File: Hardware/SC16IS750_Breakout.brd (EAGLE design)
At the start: 27.9 x 22.9 mm, 17 parts, among them IC1 SC16IS750, Q1 14.7456MHz, U1 3.3V

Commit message: Fixed board files
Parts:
- added U$2: (no value), SparkFun-Aesthetics:CREATIVE_COMMONS
- C1, C2, C4: device SparkFun:0402-CAP -> SparkFun-Passives:0603-CAP
- IC1: device SparkFun:QFN-24 -> SparkFun-DigitalIC:QFN-24
- R1, R2, R3: device SparkFun:0402-RES -> SparkFun-Passives:0603-RES
- moved C2 1.27 mm to (5.08, 14.0)
- moved R1 1.00 mm to (10.2, 12.4)
- turned C1 to 90 degrees
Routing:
- net N$24: track 9.98 -> 12.3 mm
- net N$23: track 11.0 -> 12.4 mm
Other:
- board text added: "C. Taylor, Updated by: T. Klopfenstein"

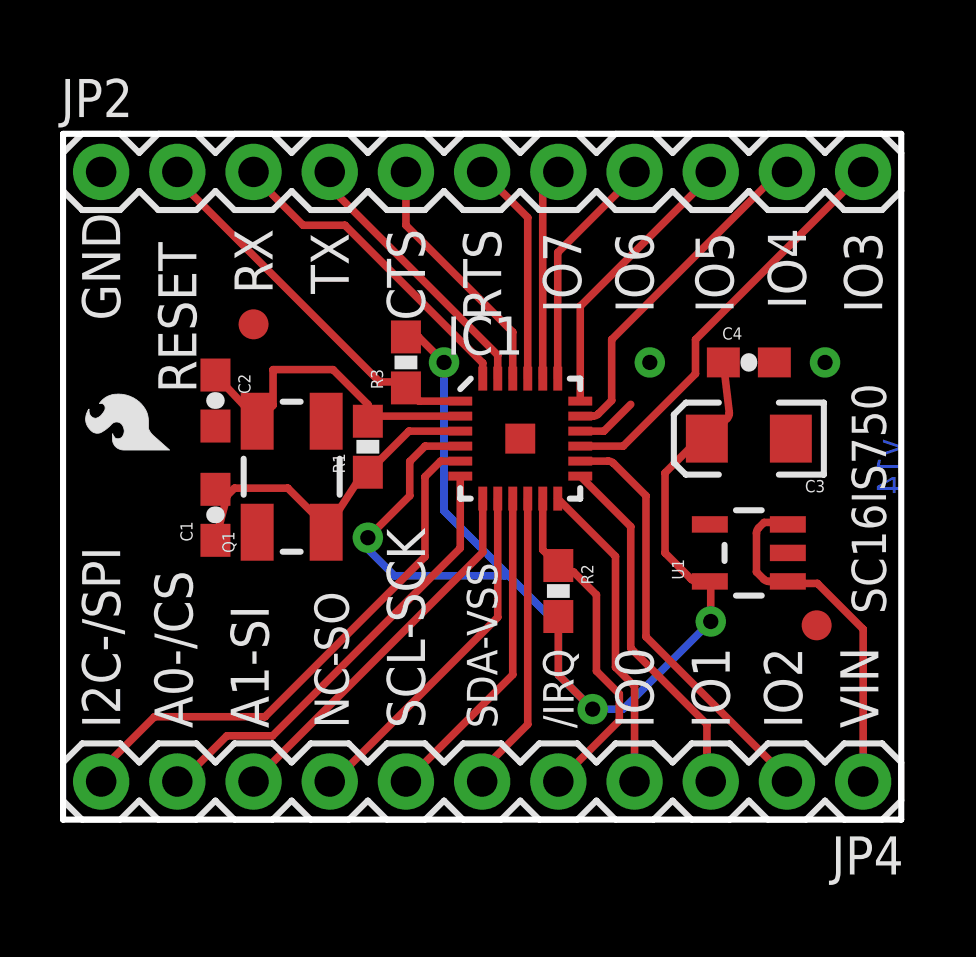
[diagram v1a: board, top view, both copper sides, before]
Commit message: Fixed traces that were crooked
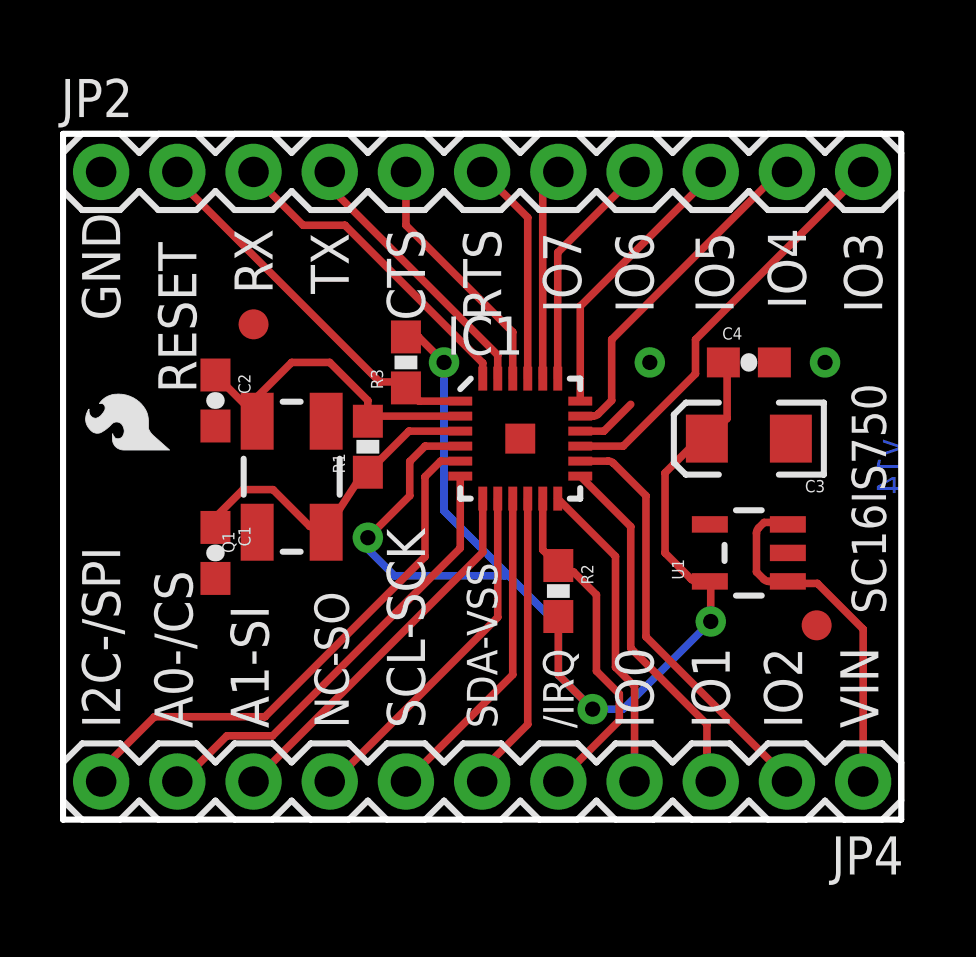
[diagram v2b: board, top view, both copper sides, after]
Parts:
- moved C1 1.27 mm to (5.08, 8.89), turned to 270 degrees

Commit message: Updated Package to "1:1" and rerouted traces directly away from IC
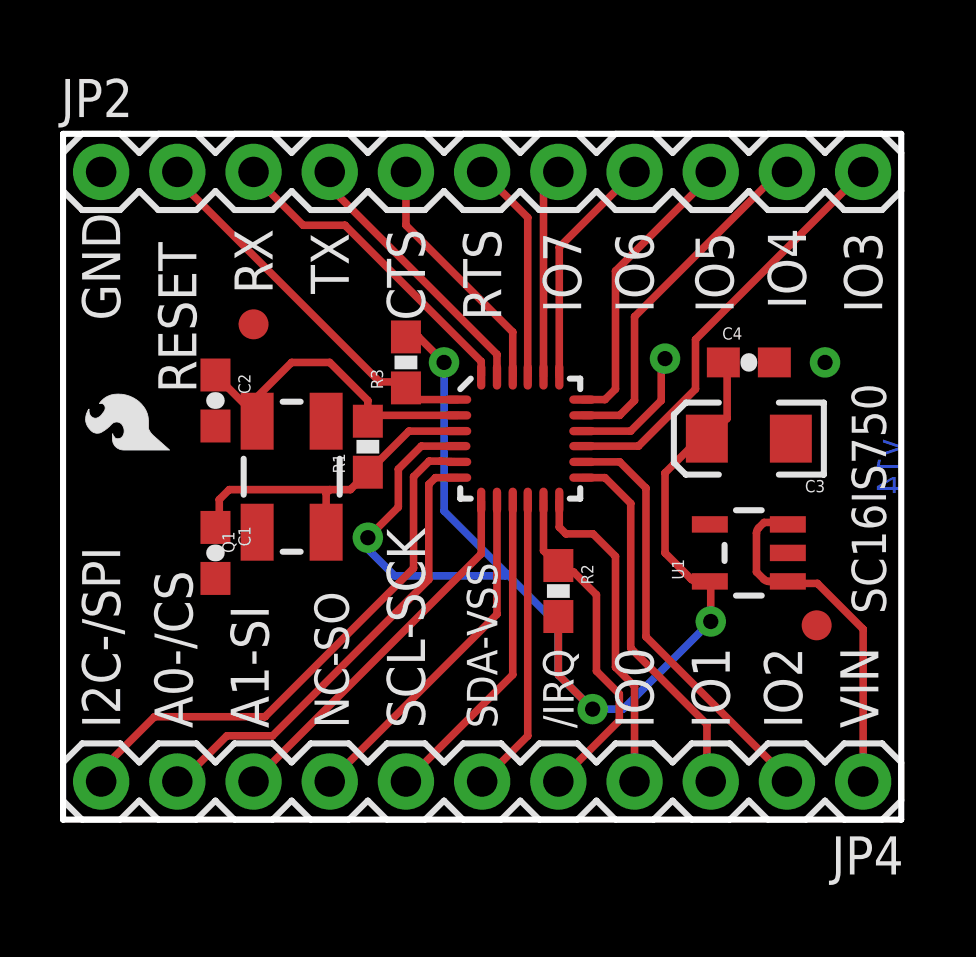
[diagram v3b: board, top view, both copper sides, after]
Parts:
- IC1: value SC16IS750 -> SC16IS7501:1; device SparkFun-DigitalIC:QFN-24 -> Testing:QFN-24_1:1
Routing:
- net GND: track 2.05 -> 4.49 mm
